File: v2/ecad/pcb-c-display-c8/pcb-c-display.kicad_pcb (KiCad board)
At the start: 4 copper layers, 344 x 228 mm, 192 parts, among them Q1 AO3401A P-FET high side, Q2 2N7002, Q3 2N7002, Q4 2N7002, Q5 AO3401A P-FET: the e-paper's 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, Q6 Si1308EDL class N-FET (RDS un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, U1 PCA9555PW 0x22: LED sinks, li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, U2 PCA9555PW 0x23: LED sinks, th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, U3 RP2040 panel controller (USB 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, U4 W25Q16JVUXIQ 16 Mbit QSPI fla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, U5 TLV75533PDBV 3.3 V 500 mA LDO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, U6 USBLC6-2SC6, U7 USBLC6-2SC6, U8 USBLC6-2SC6, U9 74LVC1G34 non-inverting buffe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, Y1 12 MHz ABM8-272-T3 (3225): 1 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

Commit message: chore(ecad): fetch B19 and C10's current boards off the box for the review set [MESHSAT-862]
Board D is byte identical on both sides and was not fetched. The two that moved:

C10, the phase board after its finish: hard 0 of the fifteen types, 1 unrouted. Its remaining open is /+3V3
at U3 pad 10, and the closure that took it from 2 to 1 was laid at 0.25 mm by a stub router whose class
lookup was dead, against the 0.5 mm its RAIL class declares. At the real class width that connection does not
fit, so read this board as two connections open, not one.

B19 as it currently stands: hard 30 (clearance 14, shorting_items 8, solder_mask_bridge 8), 499 unrouted,
which is the board AFTER the pair pre-router laid 37 of 113 pairs. The PLACED board underneath it, before any
pair copper, is hard 0, measured this morning once decision 13's region resizes landed, against 150 on 12
September. So the thirty are in the pair copper, which is the thing under investigation, and they are not the
placement. B has never been routed.

Both are committed because a board that exists only in a rented box's directory exists nowhere, which this
project learnt on 10 September by losing four routed boards to a destroyed box.
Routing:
- net /+5V: track 0.00 -> 788.2 mm, vias 0 -> 6
- net /+3V3: track 28.8 -> 790.6 mm, vias 17 -> 22
- net /LED_RAIL_SW: track 0.00 -> 731.8 mm, vias 0 -> 7
- net /LIGHT_NIGHT_n: track 2.47 -> 687.9 mm, vias 1 -> 2
- net /LIGHT_DAY_n: track 1.64 -> 679.6 mm, vias 1 -> 5
- net /ZEROIZE_HW: track 1.52 -> 651.6 mm, vias 1 -> 11
- net /TX_INHIBIT_n: track 0.00 -> 607.5 mm, vias 0 -> 12
- net /PWM1: track 1.52 -> 600.9 mm, vias 1 -> 2
- net /SLOT_EN1: track 1.52 -> 596.7 mm, vias 1 -> 5
- net /SLOT_EN3: track 1.52 -> 579.8 mm, vias 1 -> 7
- net /SOS_SW: track 1.52 -> 569.9 mm, vias 1 -> 7
- net /PI_KILL: track 1.52 -> 566.8 mm, vias 1 -> 5
- net /SHORE_INHIBIT: track 0.74 -> 555.3 mm, vias 1 -> 3
- net /SLOT_EN2: track 0.74 -> 555.2 mm, vias 1 -> 4
- net /EPD_VGL: track 3.31 -> 534.6 mm, vias 1 -> 5
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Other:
- board text added: "PCB-C C10 BACKER RING - under the face plate - MESHSAT-830"
- board text removed: "PCB-C C9 BACKER RING - under the face plate - MESHSAT-830"

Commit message: perf(pcb-c): the pre-lay is measured twice and declared for no board; C14's board stands at 0 hard and 2 unrouted [MESHSAT-862]
C15 pre-laid /EPD_SDA alone and ended at 8 open against C14's 2. C16 pre-laid the whole six-wire e-paper
bus, 5 of 7 pairs laid on the placed board, and routed 15 and 16 open against C14's 12 and 4. A lane taken by
hand on a board whose strips are its only corridors is a lane the router loses, and it loses two or three
more for it. The stage stays for a board that measures otherwise; today none does, and the rule says so
with both numbers.

C14's board is committed, sha256 c23512db603477852b4f: 0 hard, 2 unrouted, /EPD_SDA at 249 mm and /HB3 to
its test point 57 mm from the net. Decision 26 carries the six routes in one table. The test-point placement
is C's next generator change; the corridor is the owner's.
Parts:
- Q6: value Si1308EDL class N-FET (RDS under 200 mOhm, VGS 2.5 V): the boost switch on GDR -> Si2302CDS-T1-GE3 logic-level N-FET (Vishay, SOT-23, G S D like the 2N7002 symbol; VGS(th) 0.45 to 1.0 V, RDS 85 mOhm at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
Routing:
- net /EPD_SDA: track 357.8 -> 2.70 mm, vias 3 -> 0
- net /HDMI_SEL1: track 460.5 -> 581.2 mm, vias 7 -> 5
- net /HB3: track 518.4 -> 403.2 mm
- net /HDMI_SEL2: track 462.7 -> 575.0 mm, vias 4 -> 6
- net /EPD_VGH: track 467.7 -> 576.7 mm, vias 5 -> 3
- net /USB_PNL_N: track 442.1 -> 537.0 mm, vias 2 -> 13
- net /PI_KILL: track 566.8 -> 645.7 mm, vias 5 -> 4
- net /TX_INHIBIT_n: track 607.5 -> 681.9 mm, vias 12 -> 7
- net /SLOT_EN3: track 579.8 -> 511.1 mm, vias 7 -> 4
- net /PI_SHDN_REQ: track 478.7 -> 543.5 mm, vias 2 -> 6
- net /HB1: track 483.8 -> 543.0 mm, vias 4 -> 7
- net /C_RUN: track 145.3 -> 202.5 mm, vias 7 -> 8
- net /SLOT_EN2: track 555.2 -> 499.2 mm, vias 4 -> 7
- net /SOS_SW: track 569.9 -> 517.4 mm
- net /SCL: track 528.0 -> 477.8 mm, vias 9 -> 8
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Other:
- board text added: "PCB-C C14 BACKER RING - under the face plate - MESHSAT-830"
- board text removed: "PCB-C C10 BACKER RING - under the face plate - MESHSAT-830"

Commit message: fix(c): C17 routed to 0 hard and 0 unrouted with the test points beside their nets; the sounder, the headset jacks and the camera holes declared, the EMCON buffer's code read back [MESHSAT-862]
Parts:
- TP26, TP27: moved to F.Cu
- moved TP26 278.4 mm to (187.5, 104.6)
- moved TP27 278.4 mm to (191.3, 104.6)
- moved TP1 210.7 mm to (462.0, 128.0)
- moved TP2 210.6 mm to (465.5, 128.0)
- moved TP3 203.9 mm to (462.0, 131.5)
- moved TP4 203.8 mm to (465.5, 131.5)
- moved TP17 199.2 mm to (462.0, 156.0)
- moved TP18 199.1 mm to (465.5, 156.0)
- moved TP5 197.2 mm to (462.0, 135.0)
- moved TP6 197.1 mm to (465.5, 135.0)
- moved TP19 191.9 mm to (462.0, 159.5)
- moved TP20 191.7 mm to (465.5, 159.5)
- moved TP7 190.6 mm to (462.0, 138.5)
- moved TP8 190.5 mm to (465.5, 138.5)
- moved TP21 184.6 mm to (462.0, 163.0)
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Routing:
- net /EPD_VGH: track 576.7 -> 63.4 mm, vias 3 -> 2
- net /EPD_VGL: track 565.4 -> 87.0 mm, vias 5 -> 1
- net /EPD_SDA: track 2.70 -> 359.8 mm, vias 0 -> 5
- net /PI_KILL: track 645.7 -> 471.8 mm
- net /SLOT_EN1: track 601.6 -> 464.5 mm, vias 8 -> 3
- net /LED_RAIL: track 153.9 -> 281.5 mm, vias 2 -> 3
- net /HDMI_SEL1: track 581.2 -> 455.0 mm, vias 5 -> 3
- net /HDMI_SEL2: track 575.0 -> 449.4 mm
- net /HB2: track 572.7 -> 462.8 mm, vias 6 -> 5
- net /SHORE_INHIBIT: track 578.0 -> 482.1 mm, vias 9 -> 4
- net /SPARE2: track 83.9 -> 179.8 mm, vias 3 -> 0
- net /SPARE4: track 55.4 -> 147.9 mm, vias 2 -> 3
- net /PI_SHDN_REQ: track 543.5 -> 456.5 mm, vias 6 -> 5
- net /TX_K: track 280.0 -> 203.6 mm, vias 7 -> 2
- net /SPARE3: track 84.1 -> 159.5 mm, vias 3 -> 0
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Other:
- board text added: "PCB-C C17 BACKER RING - under the face plate - MESHSAT-830"
- board text removed: "PCB-C C14 BACKER RING - under the face plate - MESHSAT-830"

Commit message: feat(c): C17 cut, the first C deliverable: 0 hard, 0 unrouted, check ALL PASS, 1 of 1 rails MET, netlist 852 of 852, verify_deliverable 36 of 36 [MESHSAT-862]
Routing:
- net /SCL: track 466.0 -> 465.1 mm
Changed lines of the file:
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@@
 	(segment
 		(start 282.03 305.5653)
-		(end 276.8837 310.7116)
+		(end 275.73 311)
 		(width 0.25)
 		(layer "In2.Cu")
@@
 	)
 	(segment
-		(start 276.8837 310.7116)
-		(end 275.73 311)
-		(width 0.25)
-		(layer "In2.Cu")
-		(net 4)
-	)
-	(segment
 		(start 447.56 270.45)
 		(end 448.0717 270.9617)
@@
 	(segment
 		(start 299.73 311)
-		(end 300.8837 310.7137)
+		(end 303.8626 307.7348)
 		(width 0.25)
 		(layer "In2.Cu")
@@
 	)
 	(segment
-		(start 303.8626 307.7348)
-		(end 300.8837 310.7137)
-		(width 0.25)
-		(layer "In2.Cu")
-		(net 12)
-	)
-	(segment
 		(start 417.936 307.4374)
 		(end 347.2672 307.4374)
@@
 	(segment
 		(start 441.54 269.2256)
-		(end 443.0631 270.3303)
+		(end 444.1762 270.54)
 		(width 0.25)
 		(layer "In2.Cu")
@@
 	)
 	(segment
-		(start 444.1762 270.54)
-		(end 443.8915 269.9713)
-		(width 0.25)
-		(layer "In2.Cu")
-		(net 39)
-	)
-	(segment
 		(start 441.54 269.2256)
 		(end 441.54 261.608)
@@
 	)
 	(segment
-		(start 443.8915 269.9713)
-		(end 443.0631 270.3303)
-		(width 0.25)
-		(layer "In2.Cu")
-		(net 39)
-	)
-	(segment
 		(start 447.56 273.8318)
 		(end 446.9117 273.1835)
@@
 	)
 	(segment
-		(start 460.4403 138.508)
-		(end 461.4732 137.4751)
+		(start 461.4732 137.4751)
+		(end 458.3137 138.6863)
 		(width 0.25)
 		(layer "B.Cu")
@@
 	)
 	(segment
-		(start 458.3137 138.6863)
-		(end 460.4403 138.508)
-		(width 0.25)
-		(layer "B.Cu")
-		(net 58)
-	)
-	(segment
 		(start 463.0221 138.0542)
 		(end 463.0221 138.8974)
@@
 	)
 	(segment
-		(start 424.8837 164.7116)
-		(end 425.7731 163.8222)
+		(start 425.7731 163.8222)
+		(end 423.73 165)
 		(width 0.25)
 		(layer "In2.Cu")
@@
 	)
 	(segment
-		(start 424.8837 164.7116)
-		(end 423.73 165)
-		(width 0.25)
-		(layer "In2.Cu")
-		(net 67)
-	)
-	(segment
 		(start 429.0455 238.4954)
 		(end 427.5548 239.9861)
@@
 	(segment
 		(start 437.6145 189.5865)
-		(end 439.1564 190.1005)
+		(end 450.2802 190.4542)
 		(width 0.25)
 		(layer "B.Cu")
@@
 	)
 	(segment
-		(start 450.2802 190.4542)
-		(end 439.1564 190.1005)
-		(width 0.25)
-		(layer "B.Cu")
-		(net 70)
-	)
-	(segment
 		(start 437.1005 190.1005)
 		(end 435.0334 192.1676)
@@
 	(segment
 		(start 439.098 230.286)
-		(end 438.7193 227.7532)
+		(end 438.3406 227.3745)
 		(width 0.25)
 		(layer "B.Cu")
@@
 	)
 	(segment
-		(start 438.7193 227.7532)
-		(end 438.3406 227.3745)
-		(width 0.25)
-		(layer "B.Cu")
-		(net 75)
-	)
-	(segment
 		(start 439.098 230.286)
 		(end 439.6747 232.5476)
@@
 	(segment
 		(start 438.7519 235.0004)
-		(end 439.486 234.2663)
+		(end 439.6747 233.542)
 		(width 0.25)
 		(layer "B.Cu")
@@
 	)
 	(segment
-		(start 439.486 234.2663)
-		(end 439.6747 233.542)
-		(width 0.25)
-		(layer "B.Cu")
-		(net 75)
-	)
-	(segment
 		(start 449.198 271.1)
 		(end 449.8165 271.1)
@@
 	)
 	(segment
-		(start 420.3391 276.0635)
-		(end 420.642 275.242)
+		(start 419.5751 276.0635)
+		(end 420.155 274.755)
 		(width 0.25)
 		(layer "F.Cu")
@@
 	)
 	(segment
-		(start 420.155 274.755)
-		(end 420.642 275.242)
-		(width 0.25)
-		(layer "F.Cu")
-		(net 93)
-	)
-	(segment
 		(start 463.9777 286.646)
 		(end 462.193 284.8613)
@@
 	)
 	(segment
-		(start 420.3391 276.0635)
-		(end 419.5751 276.0635)
-		(width 0.25)
-		(layer "F.Cu")
-		(net 93)
-	)
-	(segment
 		(start 419.5751 276.0635)
 		(end 418.243 274.7314)
@@
 	)
 	(segment
-		(start 148.4537 175.5441)
-		(end 147 177)
+		(start 147 177)
+		(end 174.7134 149.2844)
 		(width 0.25)
 		(layer "B.Cu")
@@
 	)
 	(segment
-		(start 148.4537 175.5441)
-		(end 174.7134 149.2844)
-		(width 0.25)
-		(layer "B.Cu")
-		(net 122)
-	)
-	(segment
 		(start 204.3802 104.5837)
 		(end 205.3708 103.5931)
@@
 	)
 	(segment
-		(start 427.0156 293.0009)
-		(end 427.0156 292.445)
+		(start 427.0156 292.445)
+		(end 426.0729 293.9436)
 		(width 0.25)
 		(layer "In2.Cu")
@@
 		(width 0.25)
 		(layer "In2.Cu")
-		(net 132)
-	)
-	(segment
-		(start 426.0729 293.9436)
-		(end 427.0156 293.0009)
-		(width 0.25)
-		(layer "In2.Cu")

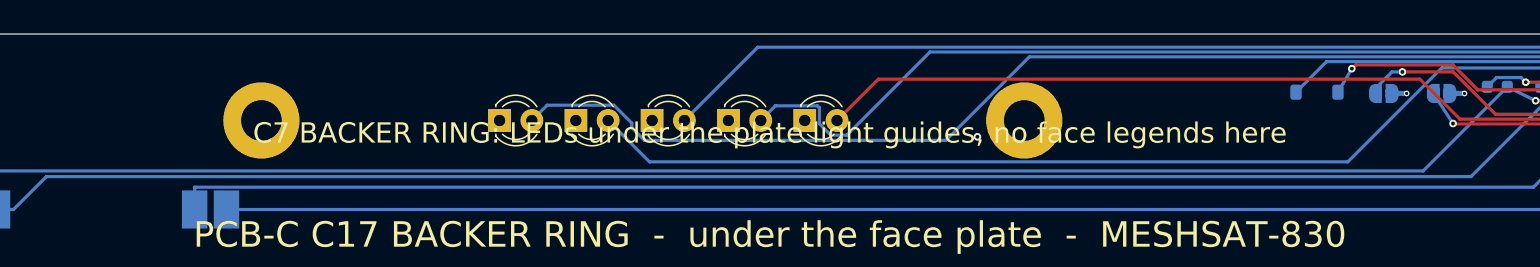
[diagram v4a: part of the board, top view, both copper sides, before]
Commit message: feat(c): C17 re-cut without the stale legend; the final gate reads the folder ALL PASS, 38 of 38, six of seven folders pass [MESHSAT-862]
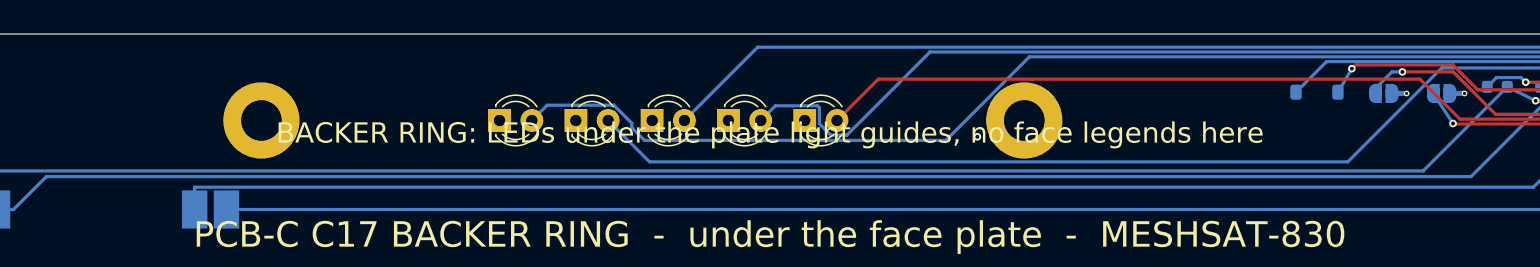
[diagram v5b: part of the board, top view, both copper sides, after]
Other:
- board text added: "BACKER RING: LEDs under the plate light guides, no face legends here"
- board text removed: "C7 BACKER RING: LEDs under the plate light guides, no face legends here"
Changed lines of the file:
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@@
 		)
 	)
-	(gr_text "C7 BACKER RING: LEDs under the plate light guides, no face legends here"
+	(gr_text "BACKER RING: LEDs under the plate light guides, no face legends here"
 		(at 297 312 0)
 		(layer "F.SilkS")
